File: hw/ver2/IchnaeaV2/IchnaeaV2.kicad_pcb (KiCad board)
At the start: 4 copper layers, 100 x 100 mm, 224 parts, among them J1 Screw_Terminal_01x09, J2 Screw_Terminal_01x09, J3 Screw_Terminal_01x09, Q1 BSS138, Q10 MCAC80N10Y, Q11 MCAC80N10Y, Q12 MCAC80N10Y, Q13 MCAC80N10Y, Q14 MCAC80N10Y, Q15 MCAC80N10Y, Q16 MCAC80N10Y, Q17 MCAC80N10Y, Q18 MCAC80N10Y, Q19 MCAC80N10Y, Q2 MCAC80N10Y, Q20 MCAC80N10Y, Q21 MCAC80N10Y, Q22 MCAC80N10Y, Q23 MCAC80N10Y, Q24 MCAC80N10Y, Q25 MCAC80N10Y, Q26 BSS138, Q27 BSS84, Q28 BSS138, Q29 BSS138, Q3 MCAC80N10Y, Q4 MCAC80N10Y, Q5 MCAC80N10Y, Q6 MCAC80N10Y, Q7 MCAC80N10Y, Q8 MCAC80N10Y, Q9 MCAC80N10Y, U1 LTC7871, U2 HIP2210, U3 HIP2210, U4 HIP2210, U5 HIP2210, U6 HIP2210, U7 HIP2210, U8 AP66200FVBW-13

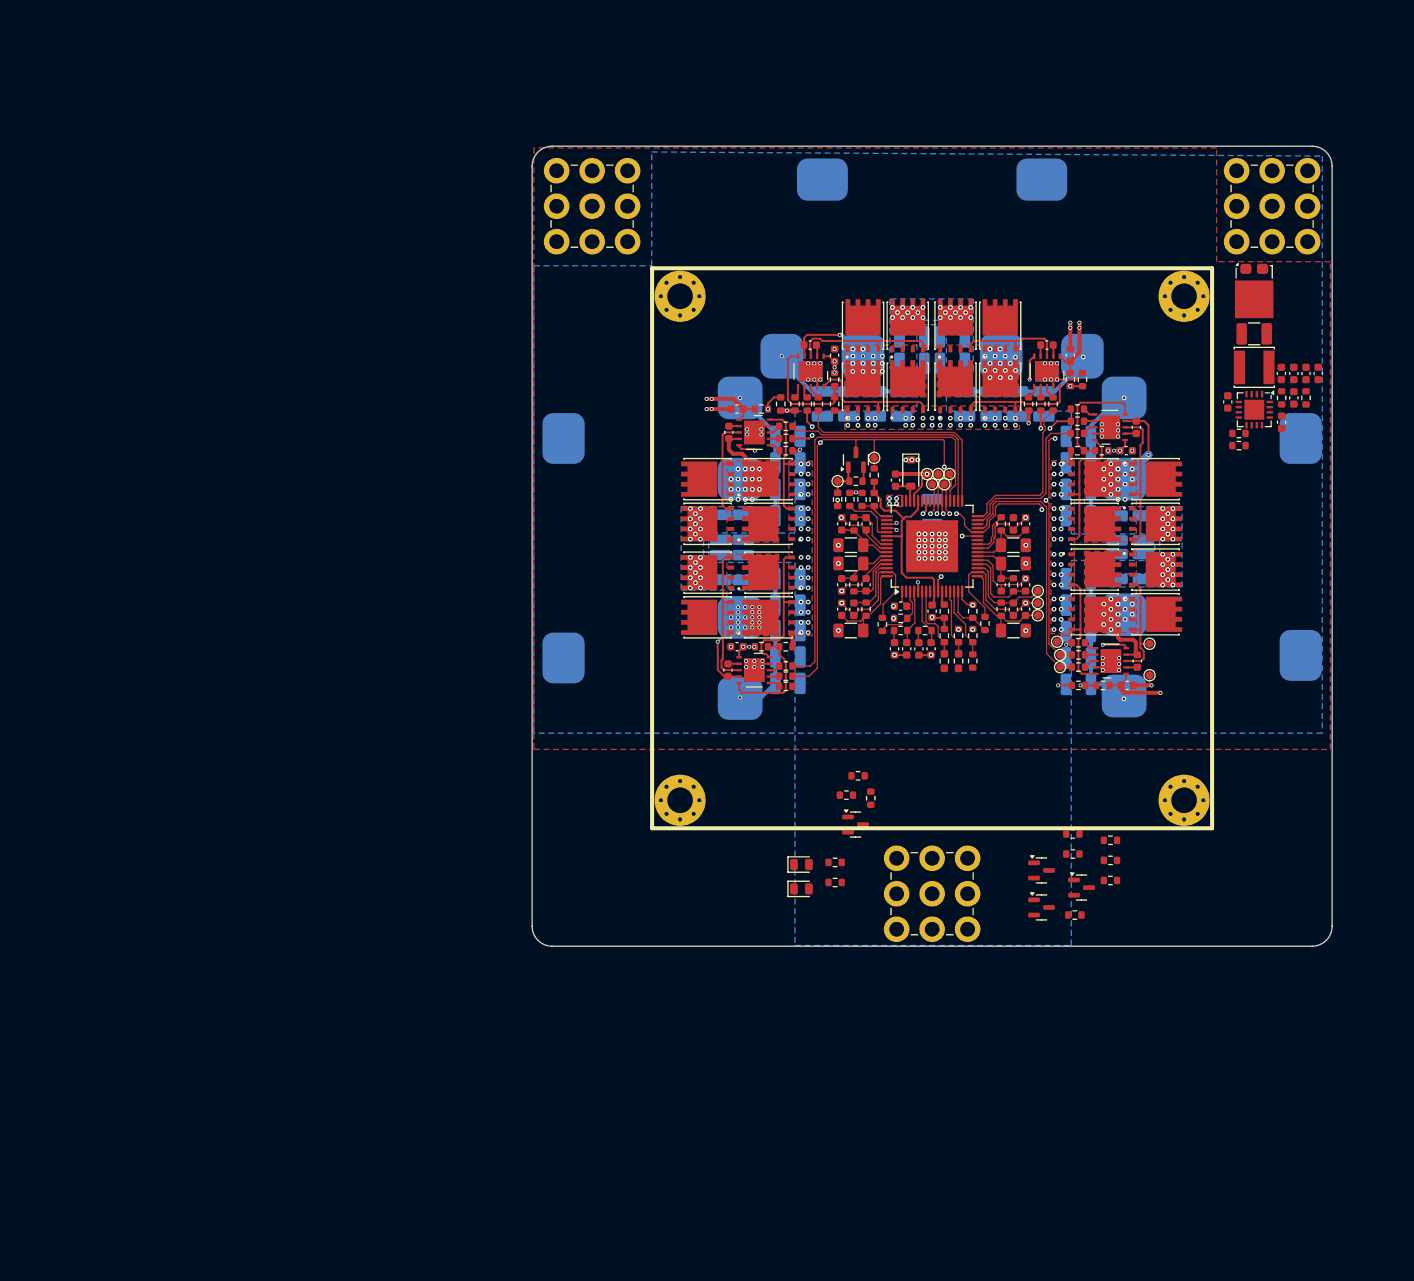
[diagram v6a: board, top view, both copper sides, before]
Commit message: Partially work through the V1 notes. Start adding some of the control stage circuitry.
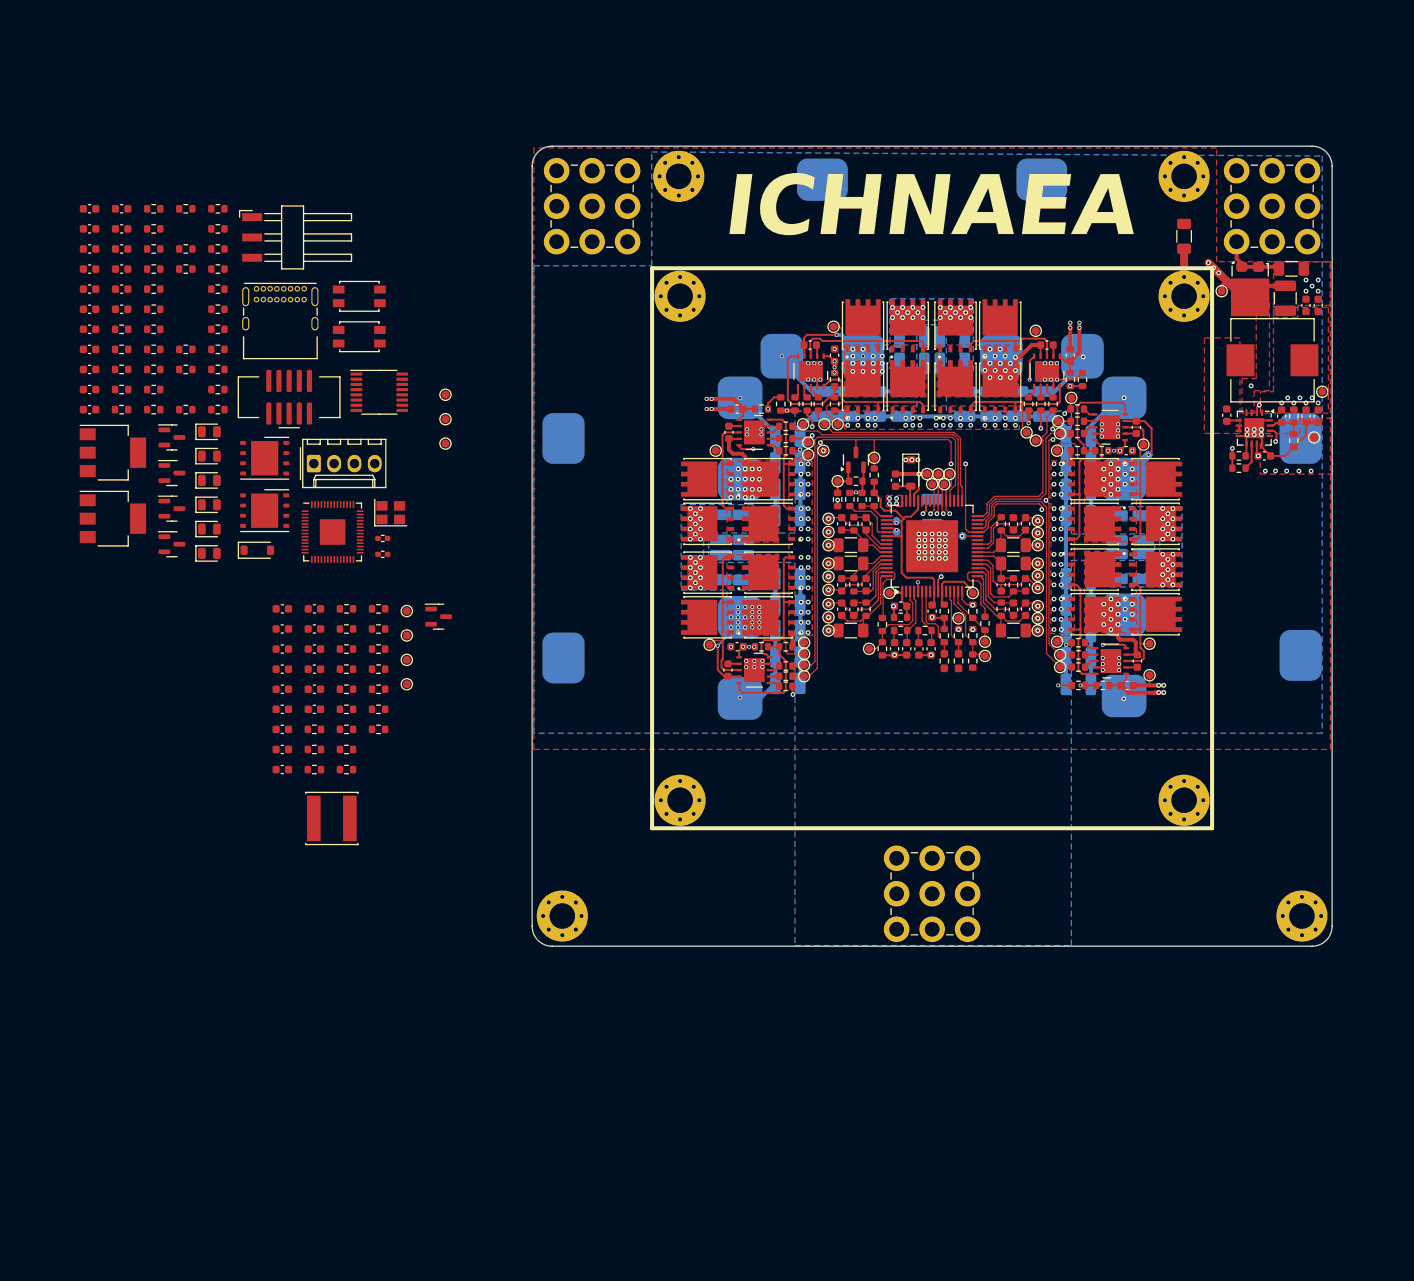
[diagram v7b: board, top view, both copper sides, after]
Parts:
- added C100: 100nF, Capacitor_SMD:C_0603_1608Metric, F.Cu at (63.8, 122.9)
- added C101: 100nF, Capacitor_SMD:C_0603_1608Metric, F.Cu at (63.8, 125.4)
- added C102: 100nF, Capacitor_SMD:C_0603_1608Metric, F.Cu at (63.8, 127.9)
- added C103: 100nF, Capacitor_SMD:C_0603_1608Metric, F.Cu at (63.8, 130.4)
- added C104: 100nF, Capacitor_SMD:C_0603_1608Metric, F.Cu at (63.8, 132.9)
- added C105: 10uF-25V, Capacitor_SMD:C_0603_1608Metric, F.Cu at (67.8, 112.8)
- added C106: 10uF-25V, Capacitor_SMD:C_0603_1608Metric, F.Cu at (67.8, 115.3)
- added C107: 10uF-25V, Capacitor_SMD:C_0603_1608Metric, F.Cu at (67.8, 117.9)
- added C108: 10uF-25V, Capacitor_SMD:C_0603_1608Metric, F.Cu at (67.8, 120.4)
- added C109: 10uF-25V, Capacitor_SMD:C_0603_1608Metric, F.Cu at (67.8, 122.9)
- added C110: 10uF-25V, Capacitor_SMD:C_0603_1608Metric, F.Cu at (67.8, 125.4)
- added C23: 100nF, Capacitor_SMD:C_0603_1608Metric, F.Cu at (39.7, 62.8)
- added C29: 100nF, Capacitor_SMD:C_0603_1608Metric, F.Cu at (39.7, 65.3)
- added C49: 15pF, Capacitor_SMD:C_0603_1608Metric, F.Cu at (39.7, 67.8)
- added C52: 15pF, Capacitor_SMD:C_0603_1608Metric, F.Cu at (39.7, 70.4)
- added C74: 100nF, Capacitor_SMD:C_0603_1608Metric, F.Cu at (39.7, 72.9)
- added C84: 100nF, Capacitor_SMD:C_0603_1608Metric, F.Cu at (39.7, 75.4)
- added C85: 10uF-25V, Capacitor_SMD:C_0603_1608Metric, F.Cu at (39.7, 77.9)
- added C86: 100nF, Capacitor_SMD:C_0603_1608Metric, F.Cu at (39.7, 80.4)
- added C87: 10uF-25V, Capacitor_SMD:C_0603_1608Metric, F.Cu at (39.7, 82.9)
- added C88: 100nF, Capacitor_SMD:C_0603_1608Metric, F.Cu at (39.7, 85.4)
- added C89: 100nF, Capacitor_SMD:C_0603_1608Metric, F.Cu at (39.7, 87.9)
- added C90: 10uF-25V, Capacitor_SMD:C_0603_1608Metric, F.Cu at (43.7, 62.8)
- added C91: 100nF, Capacitor_SMD:C_0603_1608Metric, F.Cu at (43.7, 65.3)
- added C92: 100nF, Capacitor_SMD:C_0603_1608Metric, F.Cu at (43.7, 67.8)
- added C93: 10uF-25V, Capacitor_SMD:C_0603_1608Metric, F.Cu at (43.7, 70.4)
- added C94: 100nF, Capacitor_SMD:C_0603_1608Metric, F.Cu at (43.7, 72.9)
- added C95: 10uF-25V, Capacitor_SMD:C_0603_1608Metric, F.Cu at (43.7, 75.4)
- added C96: 100nF, Capacitor_SMD:C_0603_1608Metric, F.Cu at (63.8, 112.8)
- added C97: 100nF, Capacitor_SMD:C_0603_1608Metric, F.Cu at (63.8, 115.3)
- added C98: 100nF, Capacitor_SMD:C_0603_1608Metric, F.Cu at (63.8, 117.9)
- added C99: 100nF, Capacitor_SMD:C_0603_1608Metric, F.Cu at (63.8, 120.4)
- added D4: PMEG10010ELRX, Diode_SMD:D_SOD-123, F.Cu at (60.6, 105.5)
- added D5: Yellow LED, LED_SMD:LED_0805_2012Metric, F.Cu at (54.7, 96.8)
- added D6: Yellow LED, LED_SMD:LED_0805_2012Metric, F.Cu at (54.7, 99.8)
- added D7: Green LED, LED_SMD:LED_0805_2012Metric, F.Cu at (54.7, 102.9)
- added D8: Green LED, LED_SMD:LED_0805_2012Metric, F.Cu at (54.7, 105.9)
- added H5: MountingHole_Pad, MountingHole:MountingHole_3.2mm_M3_Pad_Via, F.Cu at (98.8, 151.2)
- added H6: MountingHole_Pad, MountingHole:MountingHole_3.2mm_M3_Pad_Via, F.Cu at (113.3, 58.8)
- added H7: MountingHole_Pad, MountingHole:MountingHole_3.2mm_M3_Pad_Via, F.Cu at (176.5, 58.8)
- added H8: MountingHole_Pad, MountingHole:MountingHole_3.2mm_M3_Pad_Via, F.Cu at (191.2, 151.2)
- added J4: ~, Connectors:JTAG_2x05_P1_27mm_Shrouded_SMD, F.Cu at (64.6, 86.4)
- added J5: FanConnector, Connector_Molex:Molex_KK-254_AE-6410-04A_1x04_P2.54mm_Vertical, F.Cu at (67.7, 94.7)
- added J6: BMS_Serial, Connector_Harwin:Harwin_M20-89003xx_1x03_P2.54mm_Horizontal, F.Cu at (65.5, 66.4)
- added L8: 1.5mH, Inductor_SMD:L_Changjiang_FNR6045S, F.Cu at (70.0, 139.0)
- added P1: USB_C_Plug_USB2.0, Connector_USB:USB_C_Receptacle_GCT_USB4085, F.Cu at (60.6, 72.8)
- added Q30: BSS138, Package_TO_SOT_SMD:SOT-23, F.Cu at (83.3, 113.8)
- added R100: 1k, Resistor_SMD:R_0603_1608Metric, F.Cu at (55.7, 75.4)
- added R101: 1k, Resistor_SMD:R_0603_1608Metric, F.Cu at (55.7, 77.9)
- added R102: 510, Resistor_SMD:R_0603_1608Metric, F.Cu at (55.7, 80.4)
- added R103: 510, Resistor_SMD:R_0603_1608Metric, F.Cu at (55.7, 82.9)
- added R104: 510, Resistor_SMD:R_0603_1608Metric, F.Cu at (55.7, 85.4)
- added R105: 510, Resistor_SMD:R_0603_1608Metric, F.Cu at (55.7, 87.9)
- added R106: 6.2k-0.25w, Resistor_SMD:R_1206_3216Metric_Pad1.30x1.75mm_HandSolder, F.Cu at (176.5, 66.3)
- added R107: 100k, Resistor_SMD:R_0603_1608Metric, F.Cu at (71.8, 117.9)
- added R108: 100k, Resistor_SMD:R_0603_1608Metric, F.Cu at (71.8, 120.4)
- added R109: 10k, Resistor_SMD:R_0603_1608Metric, F.Cu at (71.8, 122.9)
- added R110: 10k, Resistor_SMD:R_0603_1608Metric, F.Cu at (71.8, 125.4)
- added R111: 10k, Resistor_SMD:R_0603_1608Metric, F.Cu at (71.8, 127.9)
- added R112: 10k, Resistor_SMD:R_0603_1608Metric, F.Cu at (71.8, 130.4)
- added R113: 100k, Resistor_SMD:R_0603_1608Metric, F.Cu at (71.8, 132.9)
- added R114: 100k, Resistor_SMD:R_0603_1608Metric, F.Cu at (75.8, 112.8)
- added R115: 10k, Resistor_SMD:R_0603_1608Metric, F.Cu at (75.8, 115.3)
- added R116: 100k, Resistor_SMD:R_0603_1608Metric, F.Cu at (75.8, 117.9)
- added R117: 100k, Resistor_SMD:R_0603_1608Metric, F.Cu at (75.8, 120.4)
- added R118: 100k, Resistor_SMD:R_0603_1608Metric, F.Cu at (75.8, 122.9)
- added R119: 10k, Resistor_SMD:R_0603_1608Metric, F.Cu at (75.8, 125.4)
- added R120: 100k, Resistor_SMD:R_0603_1608Metric, F.Cu at (75.8, 127.9)
- added R77: 10k, Resistor_SMD:R_0603_1608Metric, F.Cu at (47.7, 77.9)
- added R78: 470k, Resistor_SMD:R_0603_1608Metric, F.Cu at (47.7, 80.4)
- added R79: 27k, Resistor_SMD:R_0603_1608Metric, F.Cu at (47.7, 82.9)
- added R80: 10k, Resistor_SMD:R_0603_1608Metric, F.Cu at (47.7, 85.4)
- added R81: 470k, Resistor_SMD:R_0603_1608Metric, F.Cu at (47.7, 87.9)
- added R82: 15k, Resistor_SMD:R_0603_1608Metric, F.Cu at (51.7, 62.8)
- added R83: 100, Resistor_SMD:R_0603_1608Metric, F.Cu at (67.8, 127.9)
- added R84: 10k, Resistor_SMD:R_0603_1608Metric, F.Cu at (51.7, 67.8)
- added R85: 1k, Resistor_SMD:R_0603_1608Metric, F.Cu at (51.7, 70.4)
- added R86: 10k, Resistor_SMD:R_0603_1608Metric, F.Cu at (67.8, 130.4)
- added R87: 100k, Resistor_SMD:R_0603_1608Metric, F.Cu at (67.8, 132.9)
- added R88: 100k, Resistor_SMD:R_0603_1608Metric, F.Cu at (71.8, 112.8)
- added R89: 10k, Resistor_SMD:R_0603_1608Metric, F.Cu at (51.7, 80.4)
- added R90: 5.1k, Resistor_SMD:R_0603_1608Metric, F.Cu at (51.7, 82.9)
- added R91: 100k, Resistor_SMD:R_0603_1608Metric, F.Cu at (71.8, 115.3)
- added R92: 5.1k, Resistor_SMD:R_0603_1608Metric, F.Cu at (51.7, 87.9)
- added R93: 470k, Resistor_SMD:R_0603_1608Metric, F.Cu at (141.1, 113.9)
- added R94: 6.2k-0.25w, Resistor_SMD:R_1206_3216Metric_Pad1.30x1.75mm_HandSolder, F.Cu at (189.9, 70.3)
- added R95: 1k, Resistor_SMD:R_0603_1608Metric, F.Cu at (55.7, 62.8)
- added R96: 10k, Resistor_SMD:R_0603_1608Metric, F.Cu at (55.7, 65.3)
- added R97: 1k, Resistor_SMD:R_0603_1608Metric, F.Cu at (55.7, 67.8)
- added R98: 22, Resistor_SMD:R_0603_1608Metric, F.Cu at (55.7, 70.4)
- added R99: 22, Resistor_SMD:R_0603_1608Metric, F.Cu at (55.7, 72.9)
- added SW1: Boot, Button_Switch_SMD:SW_SPST_EVQP2, F.Cu at (73.4, 73.8)
- added SW2: Reset, Button_Switch_SMD:SW_SPST_EVQP2, F.Cu at (73.4, 78.8)
- added TH1: 10k-NTC, Resistor_SMD:R_0402_1005Metric_Pad0.72x0.64mm_HandSolder, F.Cu at (76.3, 104.0)
- added TH2: 10k-NTC, Resistor_SMD:R_0402_1005Metric_Pad0.72x0.64mm_HandSolder, F.Cu at (76.3, 106.0)
- added TP16: TestPoint, TestPoint:TestPoint_Pad_D1.0mm, F.Cu at (193.8, 85.7)
- added TP17: TestPoint, TestPoint:TestPoint_Pad_D1.0mm, F.Cu at (192.8, 91.4)
- added TP18: TestPoint, TestPoint:TestPoint_Pad_D1.0mm, F.Cu at (181.2, 73.1)
- added TP19: TestPoint, TestPoint:TestPoint_Pad_D1.0mm, F.Cu at (160.7, 89.4)
- added TP20: TestPoint, TestPoint:TestPoint_Pad_D1.0mm, F.Cu at (161.0, 90.9)
- added TP21: TestPoint, TestPoint:TestPoint_Pad_D1.0mm, F.Cu at (160.6, 93.1)
- added TP22: TestPoint, TestPoint:TestPoint_Pad_D1.0mm, F.Cu at (171.4, 92.3)
- added TP23: TestPoint, TestPoint:TestPoint_Pad_D1.0mm, F.Cu at (162.4, 86.5)
- added TP24: TestPoint, TestPoint:TestPoint_Pad_D1.0mm, F.Cu at (156.8, 90.8)
- added TP25: TestPoint, TestPoint:TestPoint_Pad_D1.0mm, F.Cu at (158.0, 78.1)
- added TP26: TestPoint, TestPoint:TestPoint_Pad_D1.0mm, F.Cu at (158.0, 91.8)
- added TP27: TestPoint, TestPoint:TestPoint_Pad_D1.0mm, F.Cu at (132.7, 77.6)
- added TP28: TestPoint, TestPoint:TestPoint_Pad_D1.0mm, F.Cu at (133.2, 89.8)
- added TP29: TestPoint, TestPoint:TestPoint_Pad_D1.0mm, F.Cu at (131.4, 93.1)
- added TP30: TestPoint, TestPoint:TestPoint_Pad_D1.0mm, F.Cu at (129.5, 92.0)
- added TP31: TestPoint, TestPoint:TestPoint_Pad_D1.0mm, F.Cu at (131.5, 89.8)
- added TP32: TestPoint, TestPoint:TestPoint_Pad_D1.0mm, F.Cu at (128.9, 89.8)
- added TP33: TestPoint, TestPoint:TestPoint_Pad_D1.0mm, F.Cu at (117.9, 93.1)
- added TP34: TestPoint, TestPoint:TestPoint_Pad_D1.0mm, F.Cu at (129.5, 93.6)
- added TP35: TestPoint, TestPoint:TestPoint_Pad_D1.0mm, F.Cu at (129.0, 118.5)
- added TP36: TestPoint, TestPoint:TestPoint_Pad_D1.0mm, F.Cu at (117.2, 117.3)
- added TP37: TestPoint, TestPoint:TestPoint_Pad_D1.0mm, F.Cu at (129.0, 117.1)
- added TP38: TestPoint, TestPoint:TestPoint_Pad_D1.0mm, F.Cu at (129.0, 121.3)
- added TP39: TestPoint, TestPoint:TestPoint_Pad_D1.0mm, F.Cu at (129.0, 119.9)
- added TP40: TestPoint, TestPoint:TestPoint_Pad_D1.0mm, F.Cu at (132.0, 115.5)
- added TP41: TestPoint, TestPoint:TestPoint_Pad_D1.0mm, F.Cu at (132.0, 112.2)
- added TP42: TestPoint, TestPoint:TestPoint_Pad_D1.0mm, F.Cu at (132.0, 113.9)
- added TP43: TestPoint, TestPoint:TestPoint_Pad_D1.0mm, F.Cu at (132.0, 108.8)
- added TP44: TestPoint, TestPoint:TestPoint_Pad_D1.0mm, F.Cu at (132.0, 107.2)
- added TP45: TestPoint, TestPoint:TestPoint_Pad_D1.0mm, F.Cu at (132.0, 110.5)
- added TP46: TestPoint, TestPoint:TestPoint_Pad_D1.0mm, F.Cu at (132.0, 103.2)
- added TP47: TestPoint, TestPoint:TestPoint_Pad_D1.0mm, F.Cu at (132.0, 104.9)
- added TP48: TestPoint, TestPoint:TestPoint_Pad_D1.0mm, F.Cu at (132.0, 101.6)
- added TP49: TestPoint, TestPoint:TestPoint_Pad_D1.0mm, F.Cu at (158.2, 107.2)
- added TP50: TestPoint, TestPoint:TestPoint_Pad_D1.0mm, F.Cu at (158.2, 110.2)
- added TP51: TestPoint, TestPoint:TestPoint_Pad_D1.0mm, F.Cu at (158.2, 108.7)
- added TP52: TestPoint, TestPoint:TestPoint_Pad_D1.0mm, F.Cu at (158.2, 103.3)
- added TP53: TestPoint, TestPoint:TestPoint_Pad_D1.0mm, F.Cu at (158.2, 104.9)
- added TP54: TestPoint, TestPoint:TestPoint_Pad_D1.0mm, F.Cu at (158.2, 101.8)
- added TP55: TestPoint, TestPoint:TestPoint_Pad_D1.0mm, B.Cu at (140.6, 103.2)
- added TP56: TestPoint, TestPoint:TestPoint_Pad_D1.0mm, B.Cu at (148.8, 103.7)
- added TP57: TestPoint, TestPoint:TestPoint_Pad_D1.0mm, B.Cu at (140.6, 101.8)
- added TP58: TestPoint, TestPoint:TestPoint_Pad_D1.0mm, F.Cu at (139.7, 110.8)
- added TP59: TestPoint, TestPoint:TestPoint_Pad_D1.0mm, F.Cu at (150.1, 110.8)
- added TP60: TestPoint, TestPoint:TestPoint_Pad_D1.0mm, F.Cu at (151.6, 116.9)
- added TP61: TestPoint, TestPoint:TestPoint_Pad_D1.0mm, F.Cu at (151.6, 118.7)
- added TP62: TestPoint, TestPoint:TestPoint_Pad_D1.0mm, F.Cu at (148.3, 114.0)
- added TP63: TestPoint, TestPoint:TestPoint_Pad_D1.0mm, F.Cu at (137.1, 117.8)
- added TP64: TestPoint, TestPoint:TestPoint_Pad_D1.0mm, F.Cu at (84.2, 86.1)
- added TP65: TestPoint, TestPoint:TestPoint_Pad_D1.0mm, F.Cu at (84.2, 89.1)
- added TP66: TestPoint, TestPoint:TestPoint_Pad_D1.0mm, F.Cu at (84.2, 92.2)
- added TP67: TestPoint, TestPoint:TestPoint_Pad_D1.0mm, F.Cu at (79.3, 113.1)
- added TP68: TestPoint, TestPoint:TestPoint_Pad_D1.0mm, F.Cu at (79.3, 116.2)
- added TP69: TestPoint, TestPoint:TestPoint_Pad_D1.0mm, F.Cu at (79.3, 119.2)
- added TP70: TestPoint, TestPoint:TestPoint_Pad_D1.0mm, F.Cu at (79.3, 122.3)
- added U10: W25Q32JVZP, Package_SON:WSON-8-1EP_6x5mm_P1.27mm_EP3.4x4.3mm, F.Cu at (61.6, 94.0)
- added U11: RP2040, Package_DFN_QFN:QFN-56-1EP_7x7mm_P0.4mm_EP3.2x3.2mm, F.Cu at (70.1, 103.2)
- added U12: LM1117MP-5.0, Package_TO_SOT_SMD:SOT-223-3_TabPin2, F.Cu at (42.6, 93.3)
- added U13: LM1117MP-3.3, Package_TO_SOT_SMD:SOT-223-3_TabPin2, F.Cu at (42.6, 101.6)
- added U14: W25Q32JVZP, Package_SON:WSON-8-1EP_6x5mm_P1.27mm_EP3.4x4.3mm, F.Cu at (61.6, 100.6)
- added U9: 74HC4051PW, Package_SO:TSSOP-16_4.4x5mm_P0.65mm, F.Cu at (75.9, 85.8)
- added Y1: 12MHz, Crystal:Crystal_SMD_3225-4Pin_3.2x2.5mm, F.Cu at (77.3, 100.8)
- C75: value 4.7uF -> 10uF-25V
- C78, C79, C80, C81: value 10uF -> 10uF-25V
- L7: footprint Inductors:TYS5020220M -> Inductor_SMD:L_Wuerth_HCI-1040
- R51: value 10k -> 1k
- moved R46 145.1 mm to (47.7, 62.8)
- moved R43 136.9 mm to (43.7, 82.9)
- moved R44 136.9 mm to (43.7, 85.4)
- moved R45 136.9 mm to (43.7, 87.9)
- moved R41 134.6 mm to (43.7, 77.9)
- moved R42 134.6 mm to (43.7, 80.4)
- moved Q28 123.2 mm to (50.0, 100.3)
- moved Q27 121.5 mm to (50.0, 95.9)
- moved Q26 121.4 mm to (50.0, 91.4)
- moved R49 111.8 mm to (47.7, 65.3)
- moved R51 111.4 mm to (47.7, 70.4), turned to 0 degrees
- moved R53 111.3 mm to (47.7, 72.9)
- moved R55 111.3 mm to (47.7, 75.4)
- moved R50 109.9 mm to (47.7, 67.8)
- moved Q29 92.4 mm to (50.0, 104.8)
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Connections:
- net /PowerStage/IO_LTC_CCM renamed LTC_CCM
- net /PowerStage/IO_LTC_DCCM renamed LTC_DCM
- net LTC_IMON renamed /PowerStage/IO_LTC_IMON
- Q28 pad 3: LTC_MODE -> /ControlStage/CTL_LTC_MODE
- Q29 pad 3: LTC_SYNC -> /ControlStage/CTL_LTC_SYNC
- R46 pad 2: LTC_MODE -> /ControlStage/CTL_LTC_MODE
- R49 pad 2: /PowerStage/IO_LTC_SYNC -> LTC_SYNC
- R51 pad 1: LTC_SYNC -> /ControlStage/CTL_LTC_SYNC
- TP12 pad 1: /PowerStage/Phase1/SNSD+ -> GND
- TP13 pad 1: /PowerStage/Phase1/SNSA+ -> Net-(Q2-S)
- U1 pad 27: LTC_RUN -> /PowerStage/IO_LTC_RUN
- U1 pad 51: LTC_MODE -> /PowerStage/IO_LTC_MODE
- U1 pad 52: LTC_SYNC -> /PowerStage/IO_LTC_SYNC
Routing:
- net GND: track 62.3 -> 189.4 mm, vias 179 -> 204
- net Net-(D1-K): track 4.05 -> 89.9 mm, vias 1 -> 6
- net LTC_MODE: track 29.1 -> 0.00 mm, vias 1 -> 0
- net /PowerStage/IO_LTC_MODE: track 0.00 -> 29.1 mm, vias 0 -> 1
- net LTC_RUN: track 27.5 -> 0.00 mm, vias 1 -> 0
- net /PowerStage/IO_LTC_RUN: track 0.00 -> 27.5 mm, vias 0 -> 1
- net LTC_SYNC: track 27.2 -> 0.00 mm, vias 1 -> 0
- net /PowerStage/IO_LTC_SYNC: track 0.00 -> 27.2 mm, vias 0 -> 1
- net VLOW: track 336.3 -> 357.4 mm
- net AP_VCC: track 0.00 -> 19.0 mm, vias 0 -> 3
- net Net-(Q10-S): track 26.2 -> 31.9 mm
- net LTC_SETCUR: track 1.75 -> 7.37 mm
- net Net-(Q7-G): track 16.9 -> 22.2 mm
- net Net-(Q15-G): track 17.0 -> 22.2 mm
- net Net-(U8-FB): track 0.00 -> 4.59 mm
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- added copper zone on F.Cu, net +12V
- added copper zone on In2.Cu, net GND
- added copper zone on F.Cu, net Net-(C76-Pad2)
- added copper zone on F.Cu, net Net-(D1-K)
- removed copper zone on In1.Cu, net Net-(D1-K)
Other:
- board text added: "ICHNAEA"

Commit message: More routing considerations for logic stage
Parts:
- removed D2, D3: Yellow LED, LED_SMD:LED_0805_2012Metric
- removed R53, R55: 10k, Resistor_SMD:R_0603_1608Metric
- added C111: 100nF, Capacitor_SMD:C_0603_1608Metric, F.Cu at (132.6, 134.7)
- added D11: ESD9B3.3ST5G, Diode_SMD:D_SOD-923, F.Cu at (46.7, 137.1)
- added D12: ESD9B3.3ST5G, Diode_SMD:D_SOD-923, F.Cu at (46.7, 139.0)
- added D13: ESD9B3.3ST5G, Diode_SMD:D_SOD-923, F.Cu at (46.7, 141.0)
- added D14: ESD9B3.3ST5G, Diode_SMD:D_SOD-923, F.Cu at (49.4, 135.1)
- added D15: ESD9B3.3ST5G, Diode_SMD:D_SOD-923, F.Cu at (49.4, 137.1)
- added D16: ESD9B3.3ST5G, Diode_SMD:D_SOD-923, F.Cu at (49.4, 139.0)
- added D17: ESD9B3.3ST5G, Diode_SMD:D_SOD-923, F.Cu at (49.4, 141.0)
- added D18: ESD9B3.3ST5G, Diode_SMD:D_SOD-923, F.Cu at (127.0, 167.7)
- added D19: ESD9B5.0ST5G, Diode_SMD:D_SOD-923, F.Cu at (119.7, 146.4)
- added D20: ESD9B5.0ST5G, Diode_SMD:D_SOD-923, F.Cu at (121.5, 146.4)
- added D9: ESD9B3.3ST5G, Diode_SMD:D_SOD-923, F.Cu at (46.7, 135.1)
- added J7: BMS_Serial, Connector_PinHeader_2.54mm:PinHeader_1x03_P2.54mm_Vertical, F.Cu at (102.5, 142.7)
- added JP1: SolderJumper_3_Bridged12, Jumpers:JumperSolderJumper-3_P0.5mm_Bridged12_0603, F.Cu at (134.3, 129.8)
- added JP2: SolderJumper_3_Bridged12, Jumpers:JumperSolderJumper-3_P0.5mm_Bridged12_0603, F.Cu at (134.3, 128.7)
- added JP3: SolderJumper_3_Bridged12, Jumpers:JumperSolderJumper-3_P0.5mm_Bridged12_0603, F.Cu at (136.4, 133.8)
- added JP4: SolderJumper_3_Bridged12, Jumpers:JumperSolderJumper-3_P0.5mm_Bridged12_0603, F.Cu at (136.4, 132.8)
- added R121: 100, Resistor_SMD:R_0603_1608Metric, F.Cu at (53.0, 127.6)
- added R122: 100, Resistor_SMD:R_0603_1608Metric, F.Cu at (113.5, 145.5)
- added R123: 100, Resistor_SMD:R_0603_1608Metric, F.Cu at (53.0, 132.6)
- added TP71: TestPoint, TestPoint:TestPoint_Pad_D1.0mm, F.Cu at (116.4, 163.0)
- J6: value BMS_Serial -> Debug; footprint Connector_Harwin:Harwin_M20-89003xx_1x03_P2.54mm_Horizontal -> Connector_PinHeader_2.54mm:PinHeader_1x03_P2.54mm_Vertical
- R100, R101, R97: value 1k -> 100
- moved C90 165.7 mm to (187.0, 146.0), turned to -90 degrees
- moved C93 158.4 mm to (182.8, 146.0), turned to -90 degrees
- moved R82 154.6 mm to (165.3, 167.7)
- moved R49 145.8 mm to (130.6, 185.3)
- moved R46 145.8 mm to (130.6, 182.8)
- moved R50 145.8 mm to (130.6, 187.8)
- moved R51 145.8 mm to (130.6, 190.3)
- moved R77 145.0 mm to (155.0, 175.4)
- moved R78 145.0 mm to (155.0, 177.9)
- moved R79 145.0 mm to (155.0, 180.4)
- moved R80 145.0 mm to (155.0, 182.9)
- moved R81 145.0 mm to (155.0, 185.4)
- moved U12 141.8 mm to (175.0, 144.1), turned to 180 degrees
- moved R41 137.9 mm to (135.0, 181.3)
- moved R42 137.9 mm to (135.0, 183.8)
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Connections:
- net /PowerStage/IO_LTC_PWM_EN renamed /ControlStage/CTL_LTC_PWM_EN
- net /PowerStage/IO_LTC_SDI renamed /ControlStage/CTL_OUT_SDO
- net Net-(D1-K) renamed /PowerStage/ExtVCC
- J5 pad 3: /ControlStage/FAN_SENSE -> Net-(J5-Pin_3)
- R100 pad 2: /ControlStage/UART0_TX -> /ControlStage/UART1_TX
- R101 pad 2: /ControlStage/UART0_RX -> /ControlStage/UART1_RX
- R102 pad 1: +5V -> +3.3V
- R103 pad 1: +5V -> +3.3V
- R85 pad 1: /ControlStage/SPI1_RX -> /ControlStage/CTL_IN_SDI
- TP1 pad 1: /PowerStage/IO_LTC_SCK -> /ControlStage/SPI1_SCK
- TP3 pad 1: /PowerStage/IO_LTC_SDO -> /ControlStage/CTL_IN_SDI
- TP4 pad 1: /PowerStage/IO_LTC_CSB -> /ControlStage/SPI1_CSn
- TP55 pad 1: /PowerStage/IO_LTC_SYNC -> /ControlStage/CTL_LTC_SYNC
- TP56 pad 1: /PowerStage/IO_LTC_RUN -> /ControlStage/CTL_OUT_RUN
- TP57 pad 1: /PowerStage/IO_LTC_MODE -> /ControlStage/CTL_LTC_MODE
- U1 pad 10: /PowerStage/IO_LTC_IMON -> /ControlStage/CTL_LTC_IMON
- U1 pad 27: /PowerStage/IO_LTC_RUN -> /ControlStage/CTL_OUT_RUN
- U1 pad 37: /PowerStage/IO_LTC_CSB -> /ControlStage/SPI1_CSn
- U1 pad 38: /PowerStage/IO_LTC_SDO -> /ControlStage/CTL_IN_SDI
- U1 pad 40: /PowerStage/IO_LTC_SCK -> /ControlStage/SPI1_SCK
- U1 pad 51: /PowerStage/IO_LTC_MODE -> /ControlStage/CTL_LTC_MODE
- U1 pad 52: /PowerStage/IO_LTC_SYNC -> /ControlStage/CTL_LTC_SYNC
- U11 pad 13: /ControlStage/SPI1_SCK -> unconnected-(U11-GPIO10-Pad13)
- U11 pad 14: /ControlStage/SPI1_TX -> unconnected-(U11-GPIO11-Pad14)
- U11 pad 17: unconnected-(U11-GPIO14-Pad17) -> /ControlStage/SPI1_SCK
- U11 pad 18: unconnected-(U11-GPIO15-Pad18) -> /ControlStage/SPI1_TX
- U11 pad 2: unconnected-(U11-GPIO0-Pad2) -> /ControlStage/SPI0_RX
- U11 pad 3: unconnected-(U11-GPIO1-Pad3) -> /ControlStage/SPI0_CSn
- U11 pad 31: unconnected-(U11-GPIO20-Pad31) -> /ControlStage/UART1_TX
- U11 pad 32: unconnected-(U11-GPIO21-Pad32) -> /ControlStage/UART1_RX
- U11 pad 37: /ControlStage/CTL_RUN -> unconnected-(U11-GPIO25-Pad37)
- U11 pad 4: unconnected-(U11-GPIO2-Pad4) -> /ControlStage/SPI0_SCK
- U11 pad 5: unconnected-(U11-GPIO3-Pad5) -> /ControlStage/SPI0_TX
- U14 pad 1: unconnected-(U14-~{CS}-Pad1) -> /ControlStage/SPI0_CSn
- U14 pad 2: unconnected-(U14-DO(IO1)-Pad2) -> /ControlStage/NOR_DO
- U14 pad 3: unconnected-(U14-IO2-Pad3) -> +3.3V
- U14 pad 4: unconnected-(U14-GND-Pad4) -> GND
- U14 pad 5: unconnected-(U14-DI(IO0)-Pad5) -> /ControlStage/NOR_DI
- U14 pad 6: unconnected-(U14-CLK-Pad6) -> /ControlStage/SPI0_SCK
- U14 pad 7: unconnected-(U14-IO3-Pad7) -> +3.3V
- U14 pad 8: unconnected-(U14-VCC-Pad8) -> +3.3V
- U14 pad 9: unconnected-(U14-EP-Pad9) -> GND
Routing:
- net /PowerStage/ExtVCC: track 89.9 -> 128.1 mm
- net /PowerStage/IO_LTC_SCK: track 32.8 -> 0.00 mm, vias 1 -> 0
- net /ControlStage/SPI1_SCK: track 0.00 -> 32.8 mm, vias 0 -> 1
- net /PowerStage/IO_LTC_CSB: track 32.7 -> 0.00 mm, vias 1 -> 0
- net /ControlStage/SPI1_CSn: track 0.00 -> 32.7 mm, vias 0 -> 1
- net /PowerStage/IO_LTC_SDO: track 31.8 -> 0.00 mm, vias 1 -> 0
- net /ControlStage/CTL_IN_SDI: track 0.00 -> 31.8 mm, vias 0 -> 1
- net /PowerStage/IO_LTC_MODE: track 29.1 -> 0.00 mm, vias 1 -> 0
- net /ControlStage/CTL_LTC_MODE: track 0.00 -> 29.1 mm, vias 0 -> 1
- net /PowerStage/IO_LTC_RUN: track 27.5 -> 0.00 mm, vias 1 -> 0
- net /ControlStage/CTL_OUT_RUN: track 0.00 -> 27.5 mm, vias 0 -> 1
- net /PowerStage/IO_LTC_SYNC: track 27.2 -> 0.00 mm, vias 1 -> 0
- net /ControlStage/CTL_LTC_SYNC: track 0.00 -> 27.2 mm, vias 0 -> 1
- net VLOW: track 357.4 -> 349.3 mm
- net GND: track 189.4 -> 183.5 mm
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- added copper zone on In2.Cu, net +3.3V
- added copper zone on In2.Cu, net +5V
- added copper zone on F.Cu, net VLOW
